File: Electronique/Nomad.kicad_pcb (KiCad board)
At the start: 4 copper layers, 67 x 68 mm, 62 parts, among them J1 Barrel_Jack, J2 Conn_01x04_Socket, J3 Conn_01x04_Socket, J4 Conn_01x02_Socket, J5 Conn_01x02_Socket, U2 BU18SD5WG-TL, U3 BU33SD5WG-TR, U4 XL1509-5.0, U5 PTAS2780RYAR, U6 ESP32-S3-DEVKITC-1-N8R2

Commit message: Elargissement des pistes d'alim en interne
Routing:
- net GND: vias 17 -> 33
- added copper zone on In1.Cu, net 1.8V
- added copper zone on In1.Cu, net 12V
- added copper zone on In1.Cu, net 3.3V
- added copper zone on In1.Cu, net 5V

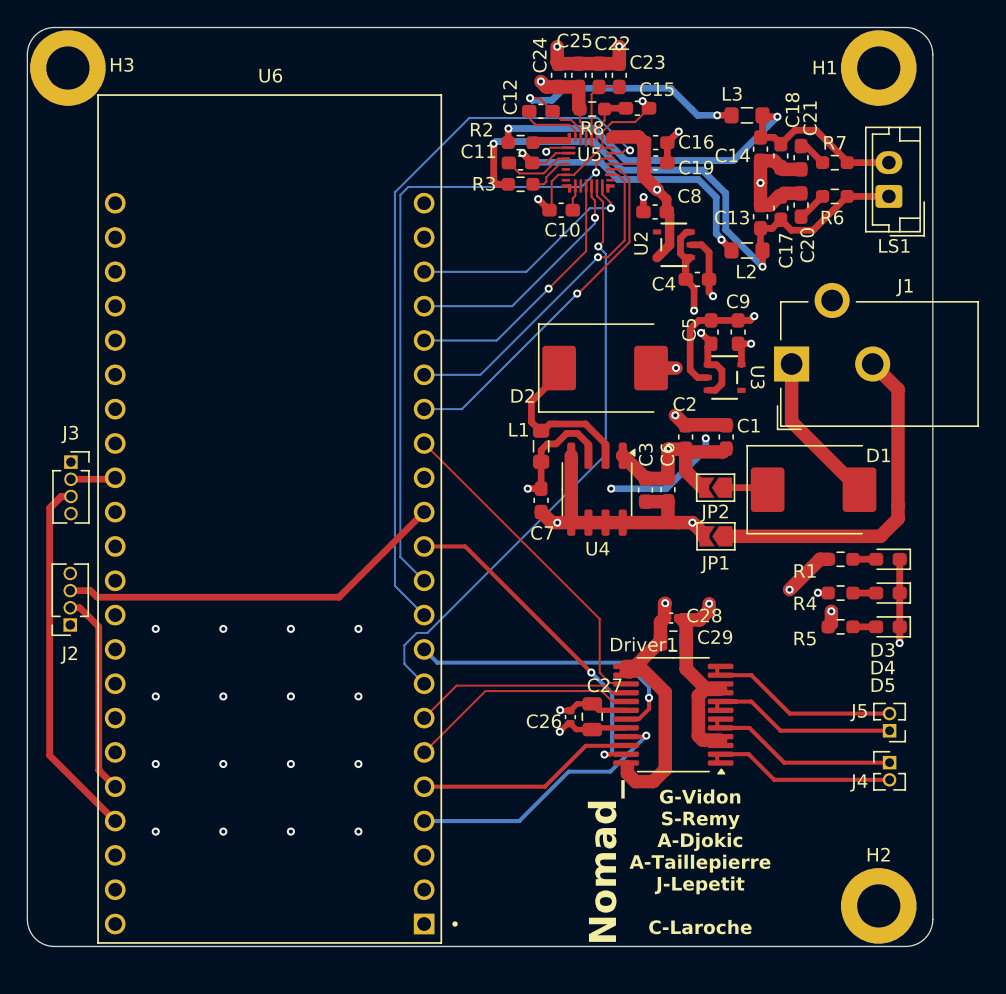
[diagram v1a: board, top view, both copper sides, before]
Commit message: Changements demandés par prof
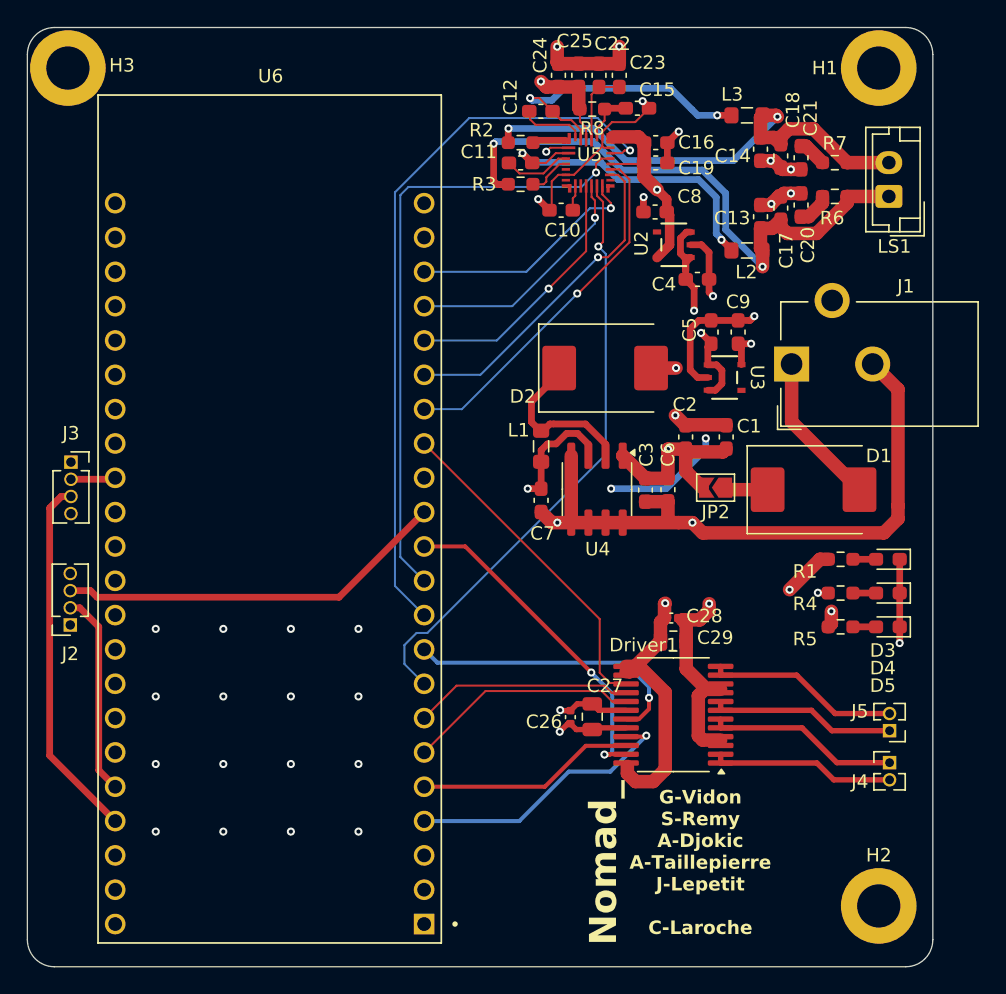
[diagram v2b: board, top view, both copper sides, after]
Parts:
- removed JP1: SolderJumper_2_Open, Jumper:SolderJumper-2_P1.3mm_Open_TrianglePad1.0x1.5mm
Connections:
- J1 pad 2: Net-(JP1-A) -> GND
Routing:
- net Net-(JP1-A): track 25.5 -> 0.00 mm
- net GND: track 125.3 -> 147.5 mm, vias 33 -> 36
- net BO2: track 15.5 -> 13.8 mm
- net /VSNS_P: track 43.1 -> 44.1 mm
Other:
- board size 67 x 68 mm -> 67 x 69.5 mm

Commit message: see prev commit message
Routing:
- net 1.8V: track 53.9 -> 56.6 mm, vias 2 -> 5
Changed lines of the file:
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@@
 	)
 	(segment
-		(start 120.312501 51.65)
-		(end 120.312501 50.712901)
-		(width 0.7)
+		(start 119.6 50.0004)
+		(end 118.634307 49.034707)
+		(width 1)
 		(layer "F.Cu")
 		(net 4)
@@
 	)
 	(segment
+		(start 122 50.0004)
+		(end 121 50.0004)
+		(width 1)
+		(layer "F.Cu")
+		(net 4)
+	)
+	(segment
+		(start 121 50.0004)
+		(end 120 50.0004)
+		(width 1)
+		(layer "F.Cu")
+		(net 4)
+	)
+	(segment
 		(start 132.494749 82.11775)
 		(end 132.262499 82.35)
@@
 	)
 	(segment
-		(start 118.634307 49.034707)
-		(end 119.6 50.0004)
-		(width 1)
-		(layer "F.Cu")
-		(net 4)
-	)
-	(segment
 		(start 118.634308 46.5202)
 		(end 118.634307 48.0202)
@@
 		(end 120.312501 51.65)
 		(width 0.7)
+		(layer "F.Cu")
+		(net 4)
+	)
+	(segment
+		(start 120 50.0004)
+		(end 119.6 50.0004)
+		(width 1)
 		(layer "F.Cu")
 		(net 4)
@@
 	)
 	(segment
-		(start 118.634307 48.0202)
-		(end 118.634307 49.034707)
-		(width 1)
-		(layer "F.Cu")
-		(net 4)
-	)
-	(segment
-		(start 120.312501 50.712901)
-		(end 119.6 50.0004)
-		(width 0.7)
+		(start 121.5 51.5)
+		(end 121.35 51.65)
+		(width 0.7)
+		(layer "F.Cu")
+		(net 4)
+	)
+	(segment
+		(start 118.634307 49.034707)
+		(end 118.634307 48.0202)
+		(width 1)
 		(layer "F.Cu")
 		(net 4)
@@
 	)
 	(segment
+		(start 121.35 51.65)
+		(end 120.312501 51.65)
+		(width 0.7)
+		(layer "F.Cu")
+		(net 4)
+	)
+	(segment
 		(start 119.59205 55.03145)
 		(end 120.52445 54.09905)
@@
 	)
 	(via
-		(at 119.6 50.0004)
+		(at 121.5 51.5)
+		(size 0.6)
+		(drill 0.3)
+		(layers "F.Cu" "B.Cu")
+		(net 4)
+	)
+	(via
+		(at 121 50.0004)
+		(size 0.6)
+		(drill 0.3)
+		(layers "F.Cu" "B.Cu")
+		(net 4)
+	)
+	(via
+		(at 120 50.0004)
+		(size 0.6)
+		(drill 0.3)
+		(layers "F.Cu" "B.Cu")
+		(net 4)
+	)
+	(via
+		(at 122 50.0004)
 		(size 0.6)
 		(drill 0.3)
@@
 		(drill 0.3)
 		(layers "F.Cu" "B.Cu")
+		(net 4)
+	)
+	(segment
+		(start 120 50.0004)
+		(end 122 50.0004)
+		(width 1)
+		(layer "In1.Cu")
+		(net 4)
+	)
+	(segment
+		(start 133 62)
+		(end 131.2 60.2)
+		(width 1)
+		(layer "In1.Cu")
+		(net 4)
+	)
+	(segment
+		(start 122 52.8)
+		(end 122 50.0004)
+		(width 1)
+		(layer "In1.Cu")
 		(net 4)
 	)
@@
 	)
 	(segment
-		(start 119.6 50.4)
-		(end 119.6 50.0004)
-		(width 1)
-		(layer "In1.Cu")
-		(net 4)
-	)
-	(segment
-		(start 133 62)
-		(end 131.2 60.2)
+		(start 129.4 60.2)
+		(end 122 52.8)
 		(width 1)
 		(layer "In1.Cu")
@@
 		(width 1)
 		(layer "In1.Cu")
-		(net 4)
-	)
-	(segment
-		(start 129.4 60.2)
-		(end 119.6 50.4)
-		(width 1)
-		(layer "In1.Cu")

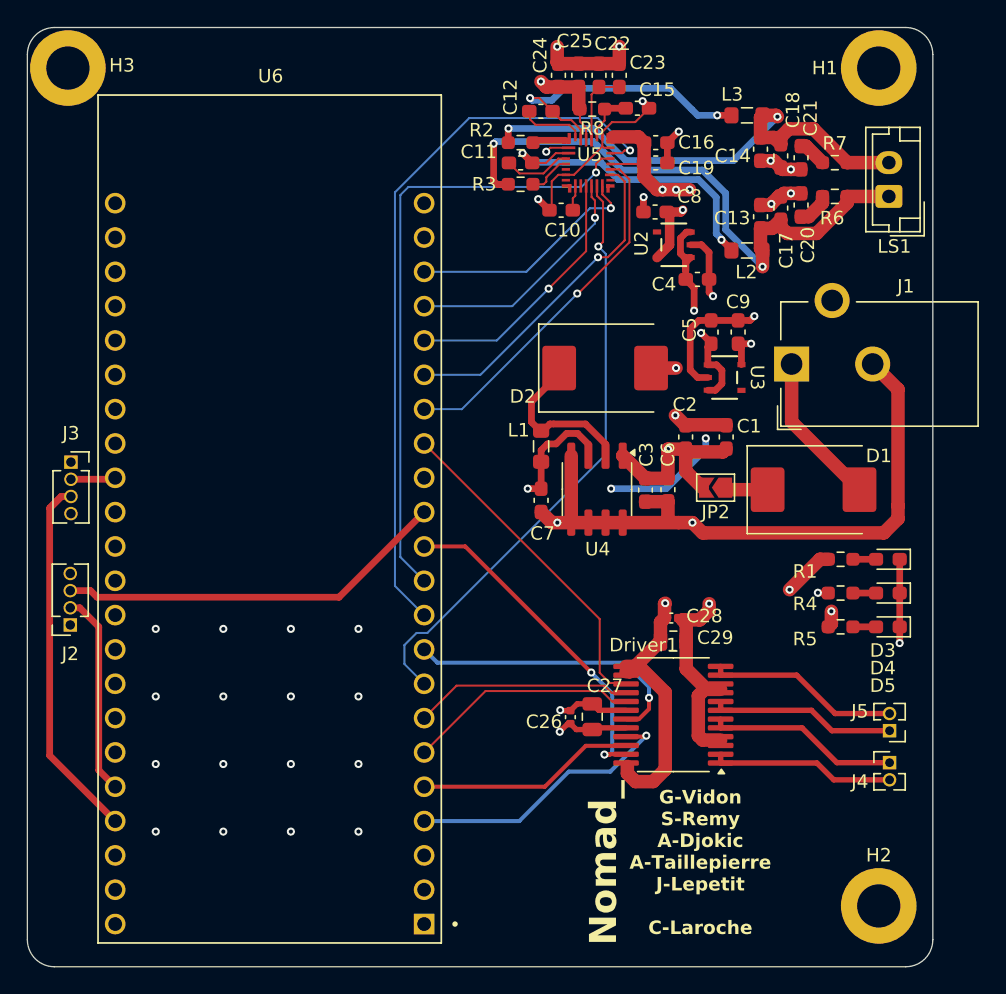
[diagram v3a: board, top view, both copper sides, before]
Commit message: PCB Finalise
finalisation pcb, création fichiers gerber
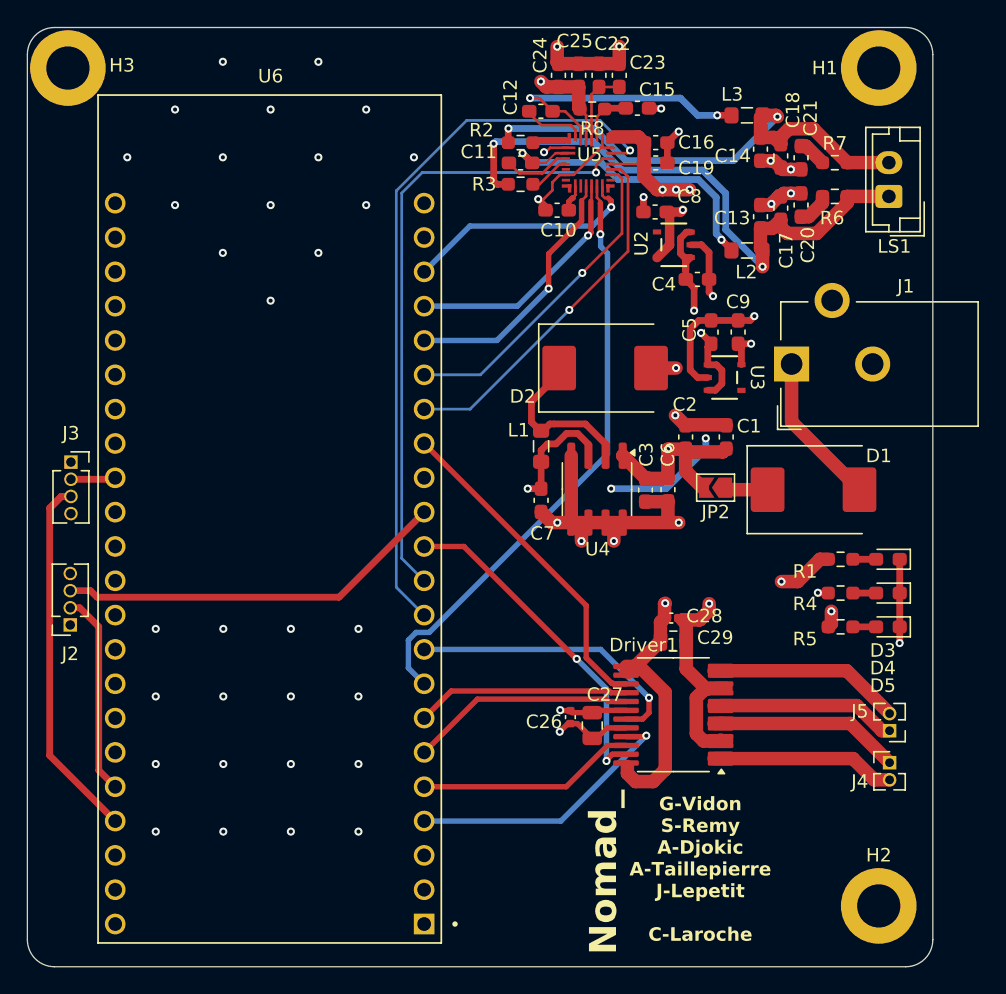
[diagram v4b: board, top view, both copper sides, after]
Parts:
- moved C27 0.65 mm to (114.8, 89.7)
- moved C10 0.30 mm to (112.2, 51.5)
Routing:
- net GND: track 147.5 -> 107.0 mm, vias 36 -> 53
- net /OUT_N: track 22.6 -> 21.0 mm
- net 5V: track 116.9 -> 118.4 mm
- net 3.3V: track 75.6 -> 74.7 mm
- net SCL: track 24.6 -> 24.1 mm
